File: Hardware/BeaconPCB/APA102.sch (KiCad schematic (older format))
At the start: 0 parts

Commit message: Added IO buffers and APA102
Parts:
- added U? (x10): APA102, symbol APA102
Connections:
- new net: U?.2 (CIN), U?.5 (COUT) (x9)
- new net: U?.1 (DIN), U?.6 (DOUT) (x9)
- new net +5V: U?.4 (VCC), U?.4 (VCC), U?.4 (VCC), U?.4 (VCC), U?.4 (VCC), U?.4 (VCC), U?.4 (VCC), U?.4 (VCC), U?.4 (VCC), U?.4 (VCC)
- new net GND: U?.3 (GND), U?.3 (GND), U?.3 (GND), U?.3 (GND), U?.3 (GND), U?.3 (GND), U?.3 (GND), U?.3 (GND), U?.3 (GND), U?.3 (GND)
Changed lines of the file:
@@
 LIBS:valves
 LIBS:STM32F042C6T6
+LIBS:crumpschemes
 LIBS:Hex-Beacons-cache
 EELAYER 25 0
 EELAYER END
-$Descr A4 11693 8268
+$Descr B 17000 11000
 encoding utf-8
 Sheet 5 5
@@
 Comment4 ""
 $EndDescr
+$Comp
+L APA102 U?
+U 1 1 59AE2A75
+P 2600 1750
+F 0 "U?" H 2300 2200 60  0000 C CNN
+F 1 "APA102" H 2800 1450 60  0000 C CNN
+F 2 "" H 2600 1300 60  0000 C CNN
+F 3 "" H 2600 1300 60  0000 C CNN
+	1    2600 1750
+	1    0    0    -1
+$EndComp
+$Comp
+L APA102 U?
+U 1 1 59AE2B3D
+P 3650 1750
+F 0 "U?" H 3350 2200 60  0000 C CNN
+F 1 "APA102" H 3850 1450 60  0000 C CNN
+F 2 "" H 3650 1300 60  0000 C CNN
+F 3 "" H 3650 1300 60  0000 C CNN
+	1    3650 1750
+	1    0    0    -1
+$EndComp
+$Comp
+L APA102 U?
+U 1 1 59AE2B99
+P 4700 1750
+F 0 "U?" H 4400 2200 60  0000 C CNN
+F 1 "APA102" H 4900 1450 60  0000 C CNN
+F 2 "" H 4700 1300 60  0000 C CNN
+F 3 "" H 4700 1300 60  0000 C CNN
+	1    4700 1750
+	1    0    0    -1
+$EndComp
+$Comp
+L APA102 U?
+U 1 1 59AE2BDC
+P 5750 1750
+F 0 "U?" H 5450 2200 60  0000 C CNN
+F 1 "APA102" H 5950 1450 60  0000 C CNN
+F 2 "" H 5750 1300 60  0000 C CNN
+F 3 "" H 5750 1300 60  0000 C CNN
+	1    5750 1750
+	1    0    0    -1
+$EndComp
+$Comp
+L APA102 U?
+U 1 1 59AE2C28
+P 6750 1750
+F 0 "U?" H 6450 2200 60  0000 C CNN
+F 1 "APA102" H 6950 1450 60  0000 C CNN
+F 2 "" H 6750 1300 60  0000 C CNN
+F 3 "" H 6750 1300 60  0000 C CNN
+	1    6750 1750
+	1    0    0    -1
+$EndComp
+$Comp
+L APA102 U?
+U 1 1 59AE2D96
+P 7750 1750
+F 0 "U?" H 7450 2200 60  0000 C CNN
+F 1 "APA102" H 7950 1450 60  0000 C CNN
+F 2 "" H 7750 1300 60  0000 C CNN
+F 3 "" H 7750 1300 60  0000 C CNN
+	1    7750 1750
+	1    0    0    -1
+$EndComp
+$Comp
+L APA102 U?
+U 1 1 59AE2D9C
+P 8800 1750
+F 0 "U?" H 8500 2200 60  0000 C CNN
+F 1 "APA102" H 9000 1450 60  0000 C CNN
+F 2 "" H 8800 1300 60  0000 C CNN
+F 3 "" H 8800 1300 60  0000 C CNN
+	1    8800 1750
+	1    0    0    -1
+$EndComp
+$Comp
+L APA102 U?
+U 1 1 59AE2DA2
+P 9850 1750
+F 0 "U?" H 9550 2200 60  0000 C CNN
+F 1 "APA102" H 10050 1450 60  0000 C CNN
+F 2 "" H 9850 1300 60  0000 C CNN
+F 3 "" H 9850 1300 60  0000 C CNN
+	1    9850 1750
+	1    0    0    -1
+$EndComp
+$Comp
+L APA102 U?
+U 1 1 59AE2DA8
+P 10900 1750
+F 0 "U?" H 10600 2200 60  0000 C CNN
+F 1 "APA102" H 11100 1450 60  0000 C CNN
+F 2 "" H 10900 1300 60  0000 C CNN
+F 3 "" H 10900 1300 60  0000 C CNN
+	1    10900 1750
+	1    0    0    -1
+$EndComp
+$Comp
+L APA102 U?
+U 1 1 59AE2DAE
+P 11900 1750
+F 0 "U?" H 11600 2200 60  0000 C CNN
+F 1 "APA102" H 12100 1450 60  0000 C CNN
+F 2 "" H 11900 1300 60  0000 C CNN
+F 3 "" H 11900 1300 60  0000 C CNN
+	1    11900 1750
+	1    0    0    -1
+$EndComp
+$Comp
+L GND #PWR?
+U 1 1 59AE6456
+P 11900 2500
+F 0 "#PWR?" H 11900 2250 50  0001 C CNN
+F 1 "GND" H 11900 2350 50  0000 C CNN
+F 2 "" H 11900 2500 50  0001 C CNN
+F 3 "" H 11900 2500 50  0001 C CNN
+	1    11900 2500
+	1    0    0    -1
+$EndComp
+$Comp
+L +5V #PWR?
+U 1 1 59AE7029
+P 2600 800
+F 0 "#PWR?" H 2600 650 50  0001 C CNN
+F 1 "+5V" H 2600 940 50  0000 C CNN
+F 2 "" H 2600 800 50  0001 C CNN
+F 3 "" H 2600 800 50  0001 C CNN
+	1    2600 800
+	1    0    0    -1
+$EndComp
+Wire Wire Line
+	2600 800  2600 1150
+Wire Wire Line
+	2600 950  11900 950
+Wire Wire Line
+	3650 950  3650 1150
+Connection ~ 2600 950
+Wire Wire Line
+	4700 950  4700 1150
+Connection ~ 3650 950
+Wire Wire Line
+	5750 950  5750 1150
+Connection ~ 4700 950
+Wire Wire Line
+	6750 950  6750 1150
+Connection ~ 5750 950
+Wire Wire Line
+	7750 950  7750 1150
+Connection ~ 6750 950
+Wire Wire Line
+	8800 950  8800 1150
+Connection ~ 7750 950
+Wire Wire Line
+	9850 950  9850 1150
+Connection ~ 8800 950
+Wire Wire Line
+	10900 950  10900 1150
+Connection ~ 9850 950
+Wire Wire Line
+	11900 950  11900 1150
+Connection ~ 10900 950
+Wire Wire Line
+	2600 2200 2600 2400
+Wire Wire Line
+	2600 2400 11900 2400
+Wire Wire Line
+	11900 2200 11900 2500
+Wire Wire Line
+	10900 2200 10900 2400
+Connection ~ 10900 2400
+Wire Wire Line
+	9850 2200 9850 2400
+Connection ~ 9850 2400
+Wire Wire Line
+	8800 2200 8800 2400
+Connection ~ 8800 2400
+Wire Wire Line
+	7750 2400 7750 2200
+Connection ~ 7750 2400
+Wire Wire Line
+	6750 2200 6750 2400
+Connection ~ 6750 2400
+Wire Wire Line
+	5750 2200 5750 2400
+Connection ~ 5750 2400
+Wire Wire Line
+	4700 2200 4700 2400
+Connection ~ 4700 2400
+Wire Wire Line
+	3650 2200 3650 2400
+Connection ~ 3650 2400
+Connection ~ 11900 2400
+Wire Wire Line
+	3200 1600 3050 1600
+Wire Wire Line
+	3050 1750 3200 1750
+Wire Wire Line
+	4100 1600 4250 1600
+Wire Wire Line
+	4100 1750 4250 1750
+Wire Wire Line
+	5150 1750 5300 1750
+Wire Wire Line
+	5300 1600 5150 1600
+Wire Wire Line
+	6200 1600 6300 1600
+Wire Wire Line
+	6200 1750 6300 1750
+Wire Wire Line
+	7200 1600 7300 1600
+Wire Wire Line
+	7200 1750 7300 1750
+Wire Wire Line
+	8200 1600 8350 1600
+Wire Wire Line
+	8200 1750 8350 1750
+Wire Wire Line
+	9250 1600 9400 1600
+Wire Wire Line
+	9250 1750 9400 1750
+Wire Wire Line
+	10300 1600 10450 1600
+Wire Wire Line
+	10300 1750 10450 1750
+Wire Wire Line
+	11350 1600 11450 1600
+Wire Wire Line
+	11350 1750 11450 1750
 $EndSCHEMATC

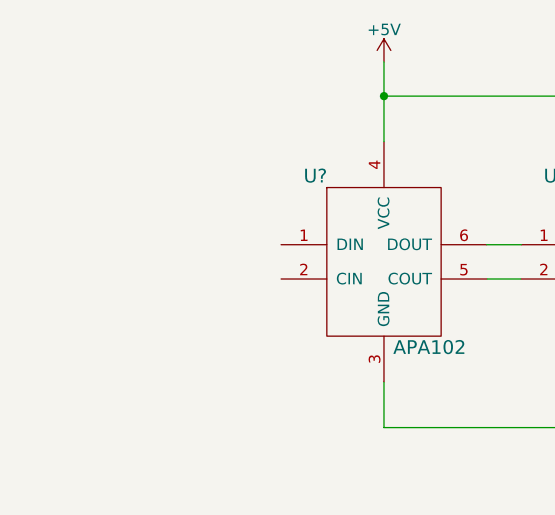
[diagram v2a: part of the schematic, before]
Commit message: Added Connectors Sheet
Started to re-arrange SPI lines
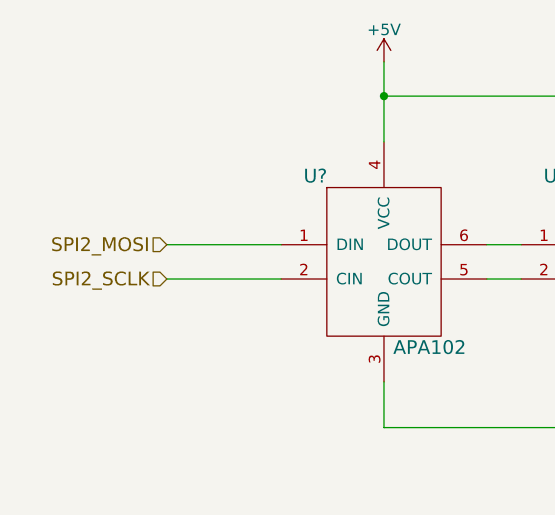
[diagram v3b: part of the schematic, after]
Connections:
- net SPI2_MOSI: now reaches U?.1 (DIN)
- net SPI2_SCLK: now reaches U?.2 (CIN)
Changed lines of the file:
@@
 $Descr B 17000 11000
 encoding utf-8
-Sheet 5 5
+Sheet 5 6
 Title ""
 Date ""
@@
 Wire Wire Line
 	11350 1750 11450 1750
+Text HLabel 1650 1600 0    60   Input ~ 0
+SPI2_MOSI
+Wire Wire Line
+	1650 1600 2150 1600
+Wire Wire Line
+	2150 1750 1650 1750
+Text HLabel 1650 1750 0    60   Input ~ 0
+SPI2_SCLK
 $EndSCHEMATC
